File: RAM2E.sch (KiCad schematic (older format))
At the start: 64 parts, among them J1 AppleIIeAux, J2 JTAG, J3 Config, U1 5M240ZT100, U2 W9864G6KH-6, U3 74AHC245, U4 74LVC245, U5 74AHC245, U6 74AHCT245, U7 74AHCT245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

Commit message: As sent to JLCPCB May 2020
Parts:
- removed J3: Config, Connector_PinHeader_2.54mm:PinHeader_2x02_P2.54mm_Vertical_SMD, symbol Connector_Generic:Conn_02x02_Odd_Even
- added SW1: Config, Button_Switch_SMD:SW_DIP_SPSTx03_Slide_6.7x9.18mm_W8.61mm_P2.54mm_LowProfile, symbol Switch:SW_DIP_x03
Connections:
- net CFG0: now also SW1.1
- net CFG1: now also SW1.2
- net GND: now also SW1.4, SW1.5, SW1.6
- net CFG2: now reaches U1.88 (IO2_88)
- net CFG2: now also SW1.3
- no-connect marks 9 -> 8
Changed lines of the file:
@@
 Text Label 7700 5550 2    50   ~ 0
 RD3
-NoConn ~ 6600 5050
 $Comp
 L power:GND #PWR0108
@@
 	1    0    0    -1
 $EndComp
-Text Label 6600 4850 0    50   ~ 0
-CFG1
-Text Label 6600 4950 0    50   ~ 0
-CFG0
-$Comp
-L Connector_Generic:Conn_02x02_Odd_Even J3
-U 1 1 5EA8BDCC
-P 7500 3950
-F 0 "J3" H 7550 4050 50  0000 C CNN
-F 1 "Config" H 7550 3750 50  0000 C CNN
-F 2 "Connector_PinHeader_2.54mm:PinHeader_2x02_P2.54mm_Vertical_SMD" H 7500 3950 50  0001 C CNN
-F 3 "~" H 7500 3950 50  0001 C CNN
-	1    7500 3950
-	1    0    0    -1
-$EndComp
-Text Label 7300 3950 2    50   ~ 0
-CFG0
-Text Label 7800 4050 0    50   ~ 0
-CFG1
-$Comp
-L power:GND #PWR0146
-U 1 1 5EAAE8A3
-P 7300 4050
-F 0 "#PWR0146" H 7300 3800 50  0001 C CNN
-F 1 "GND" H 7300 3900 50  0000 C CNN
-F 2 "" H 7300 4050 50  0001 C CNN
-F 3 "" H 7300 4050 50  0001 C CNN
-	1    7300 4050
-	1    0    0    -1
-$EndComp
-$Comp
-L power:GND #PWR0147
-U 1 1 5EAAEC35
-P 7800 3950
-F 0 "#PWR0147" H 7800 3700 50  0001 C CNN
-F 1 "GND" H 7800 3800 50  0000 C CNN
-F 2 "" H 7800 3950 50  0001 C CNN
-F 3 "" H 7800 3950 50  0001 C CNN
-	1    7800 3950
-	-1   0    0    1
-$EndComp
 $Comp
 L Device:R_Small R9
@@
 $EndComp
 $Comp
-L power:GND #PWR?
+L power:GND #PWR0148
 U 1 1 5EBEEA76
 P 950 2100
-F 0 "#PWR?" H 950 1850 50  0001 C CNN
+F 0 "#PWR0148" H 950 1850 50  0001 C CNN
 F 1 "GND" H 950 1950 50  0000 C CNN
 F 2 "" H 950 2100 50  0001 C CNN
@@
 $EndComp
 $Comp
-L power:+3V3 #PWR?
+L power:+3V3 #PWR0149
 U 1 1 5EBEF11E
 P 1350 1900
-F 0 "#PWR?" H 1350 1750 50  0001 C CNN
+F 0 "#PWR0149" H 1350 1750 50  0001 C CNN
 F 1 "+3V3" H 1350 2050 50  0000 C CNN
 F 2 "" H 1350 1900 50  0001 C CNN
@@
 Text Label 1050 1800 0    50   ~ 0
 TCK
+Text Label 6600 4850 0    50   ~ 0
+CFG1
+Text Label 6600 4950 0    50   ~ 0
+CFG0
+$Comp
+L Switch:SW_DIP_x03 SW1
+U 1 1 5EEC6E47
+P 12100 3750
+F 0 "SW1" H 12100 4100 50  0000 C CNN
+F 1 "Config" H 12100 3600 50  0000 C CNN
+F 2 "Button_Switch_SMD:SW_DIP_SPSTx03_Slide_6.7x9.18mm_W8.61mm_P2.54mm_LowProfile" H 12100 3750 50  0001 C CNN
+F 3 "~" H 12100 3750 50  0001 C CNN
+	1    12100 3750
+	1    0    0    -1
+$EndComp
+Text Label 11800 3550 2    50   ~ 0
+CFG0
+Text Label 11800 3650 2    50   ~ 0
+CFG1
+Text Label 11800 3750 2    50   ~ 0
+CFG2
+$Comp
+L power:GND #PWR0146
+U 1 1 5EEE8F32
+P 12400 3750
+F 0 "#PWR0146" H 12400 3500 50  0001 C CNN
+F 1 "GND" H 12400 3600 50  0000 C CNN
+F 2 "" H 12400 3750 50  0001 C CNN
+F 3 "" H 12400 3750 50  0001 C CNN
+	1    12400 3750
+	1    0    0    -1
+$EndComp
+Wire Wire Line
+	12400 3750 12400 3650
 Wire Bus Line
 	8200 4250 8200 5350
+Connection ~ 12400 3750
+Connection ~ 12400 3650
+Wire Wire Line
+	12400 3650 12400 3550
+Text Label 6600 5050 0    50   ~ 0
+CFG2
 $EndSCHEMATC

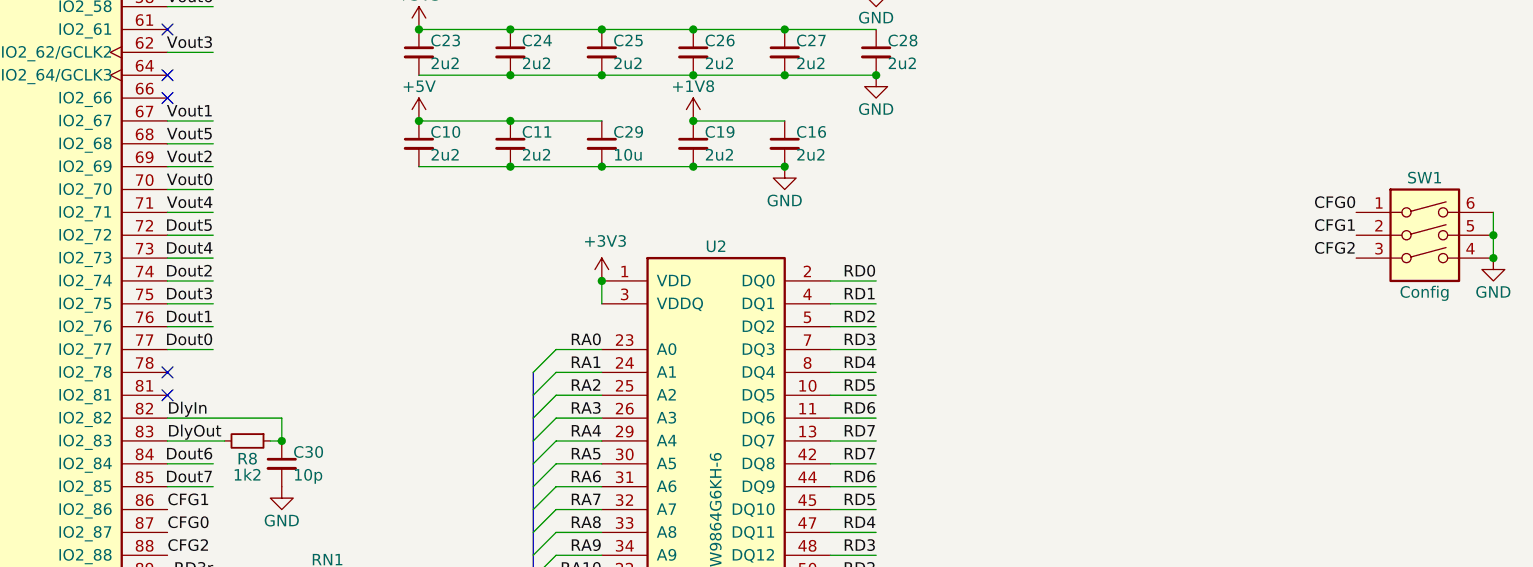
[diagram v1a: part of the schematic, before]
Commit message: Added capacity selection
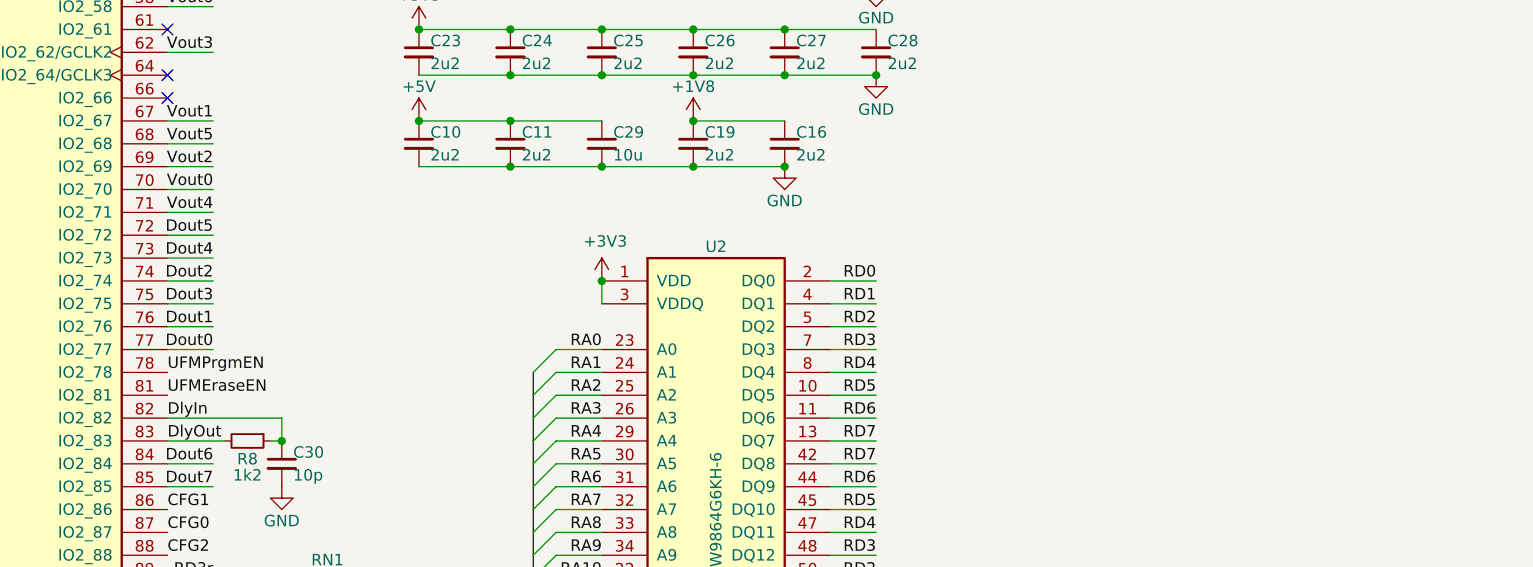
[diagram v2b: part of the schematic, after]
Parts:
- removed SW1: Config, Button_Switch_SMD:SW_DIP_SPSTx03_Slide_6.7x9.18mm_W8.61mm_P2.54mm_LowProfile, symbol Switch:SW_DIP_x03
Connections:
- net UFMPrgmEN: now reaches U1.78 (IO2_78)
- net UFMEraseEN: now reaches U1.81 (IO2_81)
- no-connect marks 8 -> 6
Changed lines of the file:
@@
 Wire Wire Line
 	6600 4450 7100 4450
-NoConn ~ 6600 4250
-NoConn ~ 6600 4350
 NoConn ~ 6600 2750
 NoConn ~ 6600 2950
@@
 Text Label 6600 4950 0    50   ~ 0
 CFG0
-$Comp
-L Switch:SW_DIP_x03 SW1
-U 1 1 5EEC6E47
-P 12100 3750
-F 0 "SW1" H 12100 4100 50  0000 C CNN
-F 1 "Config" H 12100 3600 50  0000 C CNN
-F 2 "Button_Switch_SMD:SW_DIP_SPSTx03_Slide_6.7x9.18mm_W8.61mm_P2.54mm_LowProfile" H 12100 3750 50  0001 C CNN
-F 3 "~" H 12100 3750 50  0001 C CNN
-	1    12100 3750
-	1    0    0    -1
-$EndComp
-Text Label 11800 3550 2    50   ~ 0
-CFG0
-Text Label 11800 3650 2    50   ~ 0
-CFG1
-Text Label 11800 3750 2    50   ~ 0
+Text Label 6600 5050 0    50   ~ 0
 CFG2
-$Comp
-L power:GND #PWR0146
-U 1 1 5EEE8F32
-P 12400 3750
-F 0 "#PWR0146" H 12400 3500 50  0001 C CNN
-F 1 "GND" H 12400 3600 50  0000 C CNN
-F 2 "" H 12400 3750 50  0001 C CNN
-F 3 "" H 12400 3750 50  0001 C CNN
-	1    12400 3750
-	1    0    0    -1
-$EndComp
-Wire Wire Line
-	12400 3750 12400 3650
+Text Label 6600 4250 0    50   ~ 0
+UFMPrgmEN
+Text Label 6600 4350 0    50   ~ 0
+UFMEraseEN
 Wire Bus Line
 	8200 4250 8200 5350
-Connection ~ 12400 3750
-Connection ~ 12400 3650
-Wire Wire Line
-	12400 3650 12400 3550
-Text Label 6600 5050 0    50   ~ 0
-CFG2
 $EndSCHEMATC

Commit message: Documentation update
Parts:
- C30: value 10p -> DNP
- J2: footprint Connector:Tag-Connect_TC2050-IDC-FP_2x05_P1.27mm_Vertical -> stdpads:TC2050
- R3: value 3k3 -> DNP
- R4: value 6k8 -> DNP
- R5: value DNP -> 0
- R8: value 1k2 -> DNP
- U1: value 5M240ZT100 -> EPM240T100
- U9: value TPS73701 -> DNP
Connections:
- net UFMEraseEN: no longer names the net of U1.81 (IO2_81)
- net UFMPrgmEN: no longer names the net of U1.78 (IO2_78)
- no-connect marks 6 -> 8
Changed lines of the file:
@@
 Sheet 1 2
 Title "RAM2E II"
-Date "2020-05-06"
-Rev "0.9"
+Date "2020-07-25"
+Rev "1.0"
 Comp "Garrett's Workshop"
 Comment1 ""
@@
 P 7100 4650
 F 0 "C30" H 7150 4700 50  0000 L CNN
-F 1 "10p" H 7150 4600 50  0000 L CNN
+F 1 "DNP" H 7150 4600 50  0000 L CNN
 F 2 "stdpads:C_0805" H 7100 4650 50  0001 C CNN
 F 3 "~" H 7100 4650 50  0001 C CNN
@@
 P 8450 1400
 F 0 "U9" H 8450 1600 50  0000 C CNN
-F 1 "TPS73701" H 8450 1100 50  0000 C CNN
+F 1 "DNP" H 8450 1100 50  0000 C CNN
 F 2 "stdpads:SOT-223-6" H 8450 1050 50  0001 C TNN
 F 3 "" H 8450 1250 60  0001 C CNN
@@
 P 8900 1650
 F 0 "R4" H 8850 1700 50  0000 R CNN
-F 1 "6k8" H 8850 1600 50  0000 R CNN
+F 1 "DNP" H 8850 1600 50  0000 R CNN
 F 2 "stdpads:R_0805" H 8900 1650 50  0001 C CNN
 F 3 "~" H 8900 1650 50  0001 C CNN
@@
 P 8900 1450
 F 0 "R3" H 8850 1500 50  0000 R CNN
-F 1 "3k3" H 8850 1400 50  0000 R CNN
+F 1 "DNP" H 8850 1400 50  0000 R CNN
 F 2 "stdpads:R_0805" H 8900 1450 50  0001 C CNN
 F 3 "~" H 8900 1450 50  0001 C CNN
@@
 P 10100 1050
 F 0 "R5" H 10050 1100 50  0000 R CNN
-F 1 "DNP" H 10050 1000 50  0000 R CNN
+F 1 "0" H 10050 1000 50  0000 R CNN
 F 2 "stdpads:R_0805" H 10100 1050 50  0001 C CNN
 F 3 "~" H 10100 1050 50  0001 C CNN
@@
 P 6950 4550
 F 0 "R8" V 7000 4550 50  0000 C TNN
-F 1 "1k2" V 7100 4550 50  0000 C CNN
+F 1 "DNP" V 7100 4550 50  0000 C CNN
 F 2 "stdpads:R_0805" H 6950 4550 50  0001 C CNN
 F 3 "~" H 6950 4550 50  0001 C CNN
@@
 F 0 "J2" H 1200 3000 50  0000 C CNN
 F 1 "JTAG" H 1200 2400 50  0000 C CNN
-F 2 "Connector:Tag-Connect_TC2050-IDC-FP_2x05_P1.27mm_Vertical" H 1150 2700 50  0001 C CNN
+F 2 "stdpads:TC2050" H 1150 2700 50  0001 C CNN
 F 3 "~" H 1150 2700 50  0001 C CNN
 	1    1150 2700
@@
 	1900 7050 2200 7050
 $Comp
-L GW_PLD:5M240ZT100 U1
-U 1 1 5EF407E5
-P 5600 4050
-F 0 "U1" H 5600 6631 50  0000 C CNN
-F 1 "5M240ZT100" H 5600 6540 50  0000 C CNN
-F 2 "stdpads:TQFP-100_14x14mm_P0.5mm" H 6000 1700 50  0001 L CNN
-F 3 "https://www.altera.com/content/dam/altera-www/global/en_US/pdfs/literature/hb/max2/max2_mii5v1.pdf" H 5600 4050 50  0001 C CNN
-	1    5600 4050
-	1    0    0    -1
-$EndComp
-$Comp
 L Device:R_Small R9
 U 1 1 5EBE988D
@@
 Text Label 6600 5050 0    50   ~ 0
 CFG2
-Text Label 6600 4250 0    50   ~ 0
-UFMPrgmEN
-Text Label 6600 4350 0    50   ~ 0
-UFMEraseEN
+$Comp
+L GW_PLD:5M240ZT100 U1
+U 1 1 5EF407E5
+P 5600 4050
+F 0 "U1" H 5600 6631 50  0000 C CNN
+F 1 "EPM240T100" H 5600 6540 50  0000 C CNN
+F 2 "stdpads:TQFP-100_14x14mm_P0.5mm" H 6000 1700 50  0001 L CNN
+F 3 "https://www.altera.com/content/dam/altera-www/global/en_US/pdfs/literature/hb/max2/max2_mii5v1.pdf" H 5600 4050 50  0001 C CNN
+	1    5600 4050
+	1    0    0    -1
+$EndComp
+NoConn ~ 6600 4250
+NoConn ~ 6600 4350
 Wire Bus Line
 	8200 4250 8200 5350
